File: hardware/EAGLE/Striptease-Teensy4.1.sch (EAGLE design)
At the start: 18 parts, among them IC1 74245N

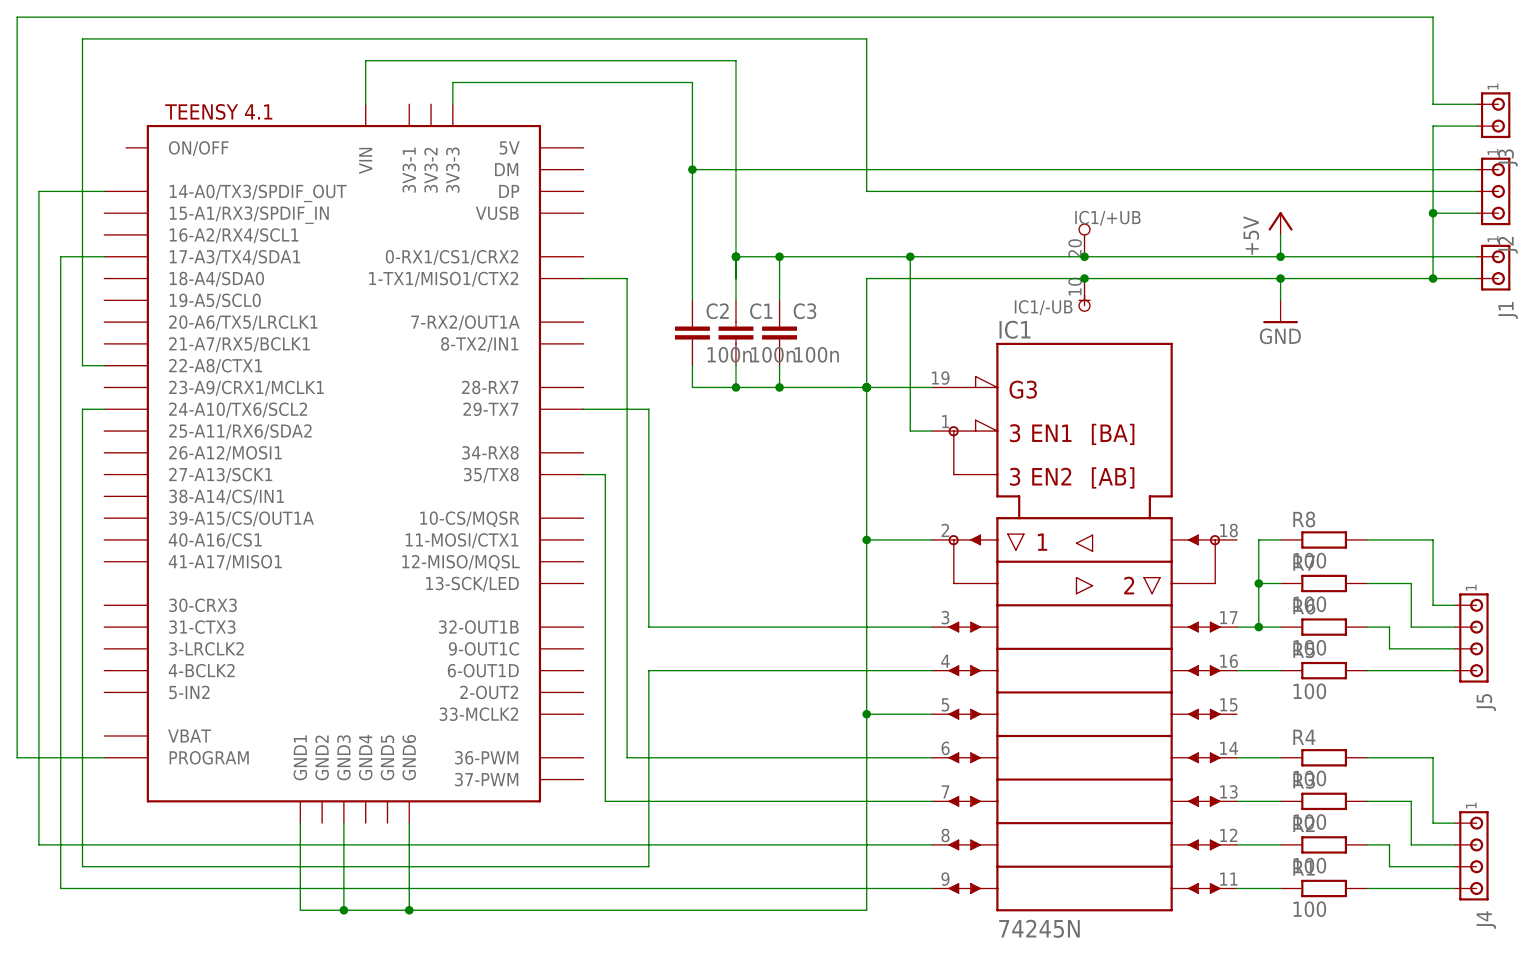
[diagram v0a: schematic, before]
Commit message: Fix circuit for Teensy 4.1.
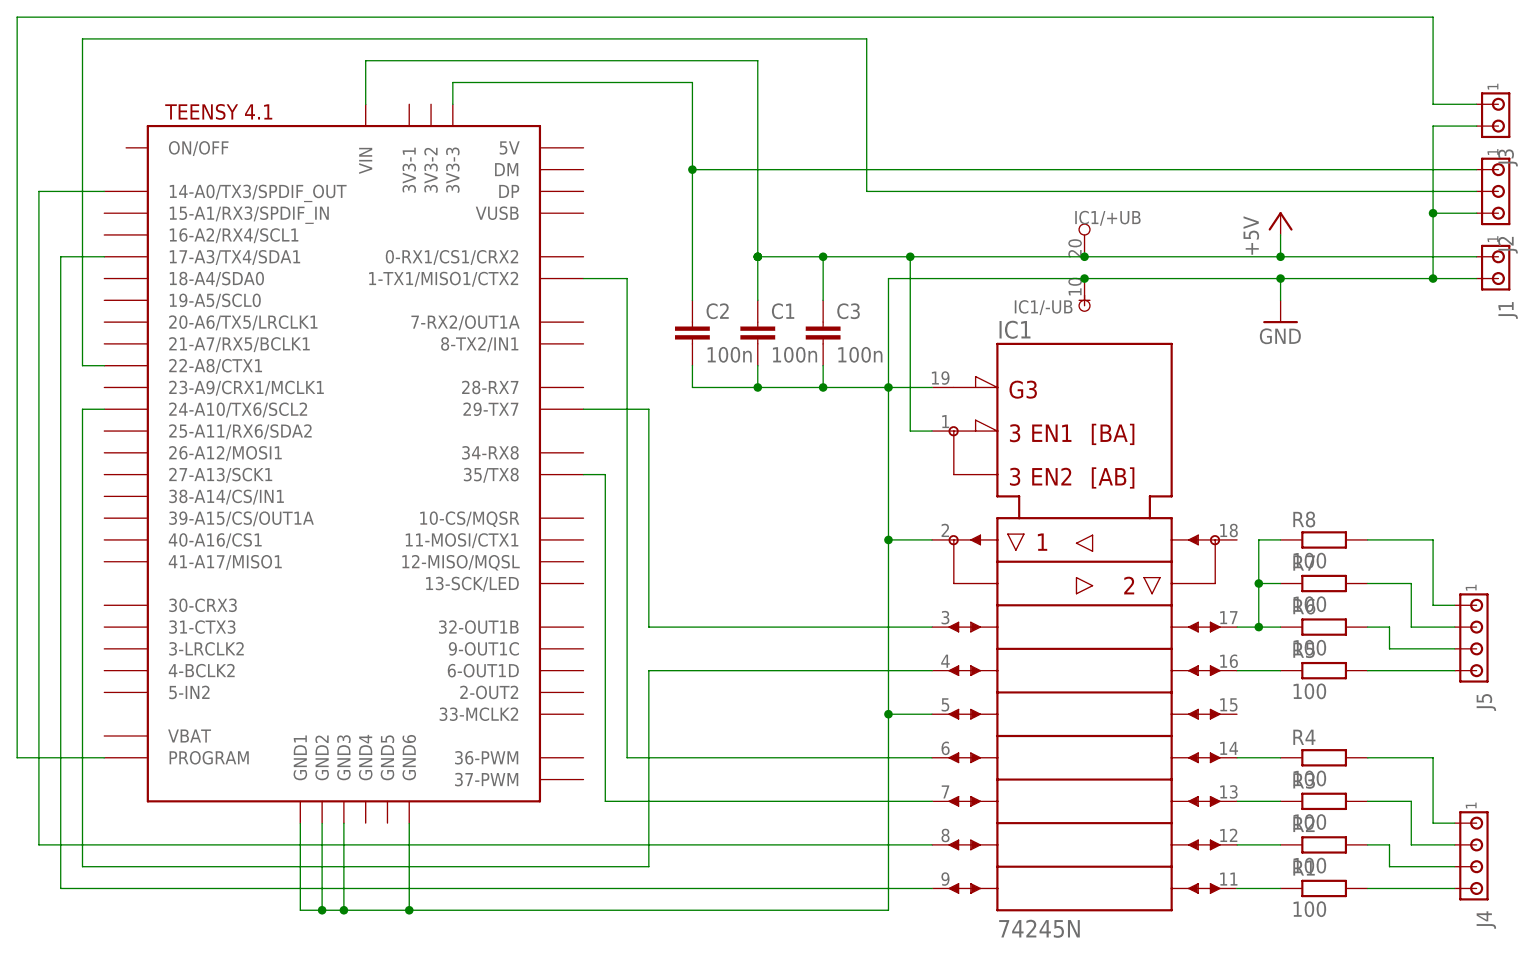
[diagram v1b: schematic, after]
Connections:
- removed net N$4: C2.2, C3.2, IC11.!G
- net GND: now also C2.2, C3.2, IC11.!G, U$3.GND2
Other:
- moved on the sheet: C1, C3
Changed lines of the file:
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@@
 <attribute name="VALUE" x="129.54" y="14.605" size="2.032" layer="96"/>
 </instance>
-<instance part="C1" gate="G$1" x="99.06" y="86.36" smashed="yes">
-<attribute name="NAME" x="100.584" y="86.741" size="1.778" layer="95"/>
-<attribute name="VALUE" x="100.584" y="81.661" size="1.778" layer="96"/>
+<instance part="C1" gate="G$1" x="101.6" y="86.36" smashed="yes">
+<attribute name="NAME" x="103.124" y="86.741" size="1.778" layer="95"/>
+<attribute name="VALUE" x="103.124" y="81.661" size="1.778" layer="96"/>
 </instance>
 <instance part="IC1" gate="/+UB" x="139.7" y="96.52" smashed="yes" rot="R180">
@@
 </instance>
 <instance part="U$3" gate="G$1" x="55.88" y="66.04" smashed="yes"/>
-<instance part="C3" gate="G$1" x="104.14" y="86.36" smashed="yes">
-<attribute name="NAME" x="105.664" y="86.741" size="1.778" layer="95"/>
-<attribute name="VALUE" x="105.664" y="81.661" size="1.778" layer="96"/>
+<instance part="C3" gate="G$1" x="109.22" y="86.36" smashed="yes">
+<attribute name="NAME" x="110.744" y="86.741" size="1.778" layer="95"/>
+<attribute name="VALUE" x="110.744" y="81.661" size="1.778" layer="96"/>
 </instance>
 <instance part="J2" gate="G$1" x="187.96" y="101.6" smashed="yes" rot="R270">
@@
 <net name="GND" class="0">
 <segment>
-<pinref part="C1" gate="G$1" pin="2"/>
-<wire x1="99.06" y1="81.28" x2="99.06" y2="78.74" width="0.1524" layer="91"/>
-<junction x="99.06" y="78.74"/>
-</segment>
-<segment>
+<pinref part="GND1" gate="1" pin="GND"/>
 <pinref part="IC1" gate="/-UB" pin="-UB"/>
+<wire x1="116.84" y1="91.44" x2="139.7" y2="91.44" width="0.1524" layer="91"/>
+<junction x="139.7" y="91.44"/>
 <wire x1="162.56" y1="91.44" x2="139.7" y2="91.44" width="0.1524" layer="91"/>
-<pinref part="GND1" gate="1" pin="GND"/>
+<pinref part="J1" gate="G$1" pin="2"/>
+<pinref part="J2" gate="G$1" pin="3"/>
+<wire x1="185.42" y1="99.06" x2="180.34" y2="99.06" width="0.1524" layer="91"/>
+<pinref part="J3" gate="G$1" pin="2"/>
+<wire x1="185.42" y1="109.22" x2="180.34" y2="109.22" width="0.1524" layer="91"/>
+<wire x1="180.34" y1="109.22" x2="180.34" y2="99.06" width="0.1524" layer="91"/>
+<junction x="180.34" y="99.06"/>
+<wire x1="180.34" y1="99.06" x2="180.34" y2="91.44" width="0.1524" layer="91"/>
+<wire x1="180.34" y1="91.44" x2="185.42" y2="91.44" width="0.1524" layer="91"/>
+<junction x="180.34" y="91.44"/>
 <wire x1="180.34" y1="91.44" x2="162.56" y2="91.44" width="0.1524" layer="91"/>
 <wire x1="162.56" y1="91.44" x2="162.56" y2="88.9" width="0.1524" layer="91"/>
-<wire x1="185.42" y1="99.06" x2="180.34" y2="99.06" width="0.1524" layer="91"/>
-<wire x1="180.34" y1="99.06" x2="180.34" y2="91.44" width="0.1524" layer="91"/>
-<junction x="114.3" y="78.74"/>
-<junction x="114.3" y="78.74"/>
+<junction x="162.56" y="91.44"/>
+<pinref part="IC1" gate="1" pin="!G"/>
+<wire x1="109.22" y1="78.74" x2="116.84" y2="78.74" width="0.1524" layer="91"/>
+<pinref part="C3" gate="G$1" pin="2"/>
+<wire x1="116.84" y1="78.74" x2="121.92" y2="78.74" width="0.1524" layer="91"/>
+<wire x1="109.22" y1="81.28" x2="109.22" y2="78.74" width="0.1524" layer="91"/>
+<junction x="109.22" y="78.74"/>
+<pinref part="C2" gate="G$1" pin="2"/>
+<wire x1="93.98" y1="81.28" x2="93.98" y2="78.74" width="0.1524" layer="91"/>
+<wire x1="93.98" y1="78.74" x2="101.6" y2="78.74" width="0.1524" layer="91"/>
+<pinref part="C1" gate="G$1" pin="2"/>
+<wire x1="101.6" y1="78.74" x2="109.22" y2="78.74" width="0.1524" layer="91"/>
+<wire x1="101.6" y1="81.28" x2="101.6" y2="78.74" width="0.1524" layer="91"/>
+<junction x="101.6" y="78.74"/>
+<wire x1="116.84" y1="91.44" x2="116.84" y2="78.74" width="0.1524" layer="91"/>
+<junction x="116.84" y="78.74"/>
 <pinref part="IC1" gate="1" pin="A1"/>
-<wire x1="114.3" y1="60.96" x2="121.92" y2="60.96" width="0.1524" layer="91"/>
-<wire x1="114.3" y1="78.74" x2="114.3" y2="91.44" width="0.1524" layer="91"/>
-<junction x="114.3" y="78.74"/>
-<wire x1="60.96" y1="27.94" x2="60.96" y2="17.78" width="0.1524" layer="91"/>
-<wire x1="60.96" y1="17.78" x2="114.3" y2="17.78" width="0.1524" layer="91"/>
-<wire x1="114.3" y1="17.78" x2="114.3" y2="40.64" width="0.1524" layer="91"/>
-<wire x1="114.3" y1="60.96" x2="114.3" y2="78.74" width="0.1524" layer="91"/>
-<wire x1="114.3" y1="60.96" x2="114.3" y2="40.64" width="0.1524" layer="91"/>
-<junction x="114.3" y="60.96"/>
+<wire x1="116.84" y1="60.96" x2="121.92" y2="60.96" width="0.1524" layer="91"/>
+<wire x1="48.26" y1="17.78" x2="50.8" y2="17.78" width="0.1524" layer="91"/>
+<wire x1="50.8" y1="17.78" x2="53.34" y2="17.78" width="0.1524" layer="91"/>
+<wire x1="53.34" y1="17.78" x2="60.96" y2="17.78" width="0.1524" layer="91"/>
+<wire x1="60.96" y1="17.78" x2="116.84" y2="17.78" width="0.1524" layer="91"/>
+<wire x1="116.84" y1="17.78" x2="116.84" y2="40.64" width="0.1524" layer="91"/>
+<wire x1="116.84" y1="60.96" x2="116.84" y2="40.64" width="0.1524" layer="91"/>
 <pinref part="IC1" gate="1" pin="A4"/>
-<wire x1="114.3" y1="40.64" x2="121.92" y2="40.64" width="0.1524" layer="91"/>
-<junction x="114.3" y="78.74"/>
-<pinref part="U$3" gate="G$1" pin="GND6"/>
-<junction x="114.3" y="40.64"/>
-<wire x1="114.3" y1="91.44" x2="139.7" y2="91.44" width="0.1524" layer="91"/>
-<junction x="139.7" y="91.44"/>
-<junction x="162.56" y="91.44"/>
-<wire x1="60.96" y1="17.78" x2="53.34" y2="17.78" width="0.1524" layer="91"/>
-<junction x="60.96" y="17.78"/>
+<wire x1="116.84" y1="40.64" x2="121.92" y2="40.64" width="0.1524" layer="91"/>
+<junction x="116.84" y="40.64"/>
 <pinref part="U$3" gate="G$1" pin="GND1"/>
-<wire x1="53.34" y1="17.78" x2="48.26" y2="17.78" width="0.1524" layer="91"/>
 <wire x1="48.26" y1="17.78" x2="48.26" y2="27.94" width="0.1524" layer="91"/>
+<wire x1="116.84" y1="78.74" x2="116.84" y2="60.96" width="0.1524" layer="91"/>
+<junction x="116.84" y="60.96"/>
+<pinref part="U$3" gate="G$1" pin="GND2"/>
+<wire x1="50.8" y1="27.94" x2="50.8" y2="17.78" width="0.1524" layer="91"/>
+<junction x="50.8" y="17.78"/>
 <pinref part="U$3" gate="G$1" pin="GND3"/>
 <wire x1="53.34" y1="27.94" x2="53.34" y2="17.78" width="0.1524" layer="91"/>
 <junction x="53.34" y="17.78"/>
-<wire x1="185.42" y1="109.22" x2="180.34" y2="109.22" width="0.1524" layer="91"/>
-<wire x1="180.34" y1="109.22" x2="180.34" y2="99.06" width="0.1524" layer="91"/>
-<junction x="180.34" y="99.06"/>
-<pinref part="J1" gate="G$1" pin="2"/>
-<wire x1="180.34" y1="91.44" x2="185.42" y2="91.44" width="0.1524" layer="91"/>
-<junction x="180.34" y="91.44"/>
-<pinref part="J2" gate="G$1" pin="3"/>
-<pinref part="J3" gate="G$1" pin="2"/>
+<pinref part="U$3" gate="G$1" pin="GND6"/>
+<wire x1="60.96" y1="27.94" x2="60.96" y2="17.78" width="0.1524" layer="91"/>
+<junction x="60.96" y="17.78"/>
 </segment>
 </net>
@@
 <net name="+5V" class="0">
 <segment>
-<wire x1="99.06" y1="93.98" x2="104.14" y2="93.98" width="0.1524" layer="91"/>
-<wire x1="104.14" y1="93.98" x2="119.38" y2="93.98" width="0.1524" layer="91"/>
+<wire x1="101.6" y1="93.98" x2="109.22" y2="93.98" width="0.1524" layer="91"/>
+<wire x1="109.22" y1="93.98" x2="119.38" y2="93.98" width="0.1524" layer="91"/>
 <wire x1="119.38" y1="93.98" x2="139.7" y2="93.98" width="0.1524" layer="91"/>
 <pinref part="IC1" gate="/+UB" pin="+UB"/>
 <junction x="139.7" y="93.98"/>
 <wire x1="139.7" y1="93.98" x2="162.56" y2="93.98" width="0.1524" layer="91"/>
-<wire x1="99.06" y1="91.44" x2="99.06" y2="93.98" width="0.1524" layer="91"/>
-<junction x="99.06" y="93.98"/>
+<junction x="101.6" y="93.98"/>
 <pinref part="C1" gate="G$1" pin="1"/>
-<wire x1="99.06" y1="88.9" x2="99.06" y2="93.98" width="0.1524" layer="91"/>
-<junction x="99.06" y="93.98"/>
+<wire x1="101.6" y1="88.9" x2="101.6" y2="93.98" width="0.1524" layer="91"/>
+<junction x="101.6" y="93.98"/>
 <pinref part="IC1" gate="1" pin="DIR"/>
 <wire x1="121.92" y1="73.66" x2="119.38" y2="73.66" width="0.1524" layer="91"/>
 <wire x1="119.38" y1="73.66" x2="119.38" y2="93.98" width="0.1524" layer="91"/>
 <junction x="119.38" y="93.98"/>
-<wire x1="55.88" y1="116.84" x2="99.06" y2="116.84" width="0.1524" layer="91"/>
+<wire x1="55.88" y1="116.84" x2="101.6" y2="116.84" width="0.1524" layer="91"/>
 <pinref part="U$3" gate="G$1" pin="VIN"/>
 <wire x1="55.88" y1="111.76" x2="55.88" y2="116.84" width="0.1524" layer="91"/>
-<wire x1="99.06" y1="116.84" x2="99.06" y2="93.98" width="0.1524" layer="91"/>
+<wire x1="101.6" y1="116.84" x2="101.6" y2="93.98" width="0.1524" layer="91"/>
 <pinref part="P+1" gate="1" pin="+5V"/>
 <wire x1="162.56" y1="93.98" x2="162.56" y2="96.52" width="0.1524" layer="91"/>
 <pinref part="C3" gate="G$1" pin="1"/>
-<wire x1="104.14" y1="88.9" x2="104.14" y2="93.98" width="0.1524" layer="91"/>
-<junction x="104.14" y="93.98"/>
+<wire x1="109.22" y1="88.9" x2="109.22" y2="93.98" width="0.1524" layer="91"/>
+<junction x="109.22" y="93.98"/>
 <pinref part="J1" gate="G$1" pin="1"/>
 <wire x1="185.42" y1="93.98" x2="162.56" y2="93.98" width="0.1524" layer="91"/>
@@
 </segment>
 </net>
-<net name="N$4" class="0">
-<segment>
-<pinref part="IC1" gate="1" pin="!G"/>
-<wire x1="104.14" y1="78.74" x2="121.92" y2="78.74" width="0.1524" layer="91"/>
-<pinref part="C3" gate="G$1" pin="2"/>
-<wire x1="104.14" y1="81.28" x2="104.14" y2="78.74" width="0.1524" layer="91"/>
-<junction x="104.14" y="78.74"/>
-<pinref part="C2" gate="G$1" pin="2"/>
-<wire x1="93.98" y1="81.28" x2="93.98" y2="78.74" width="0.1524" layer="91"/>
-<wire x1="93.98" y1="78.74" x2="104.14" y2="78.74" width="0.1524" layer="91"/>
-</segment>
-</net>
